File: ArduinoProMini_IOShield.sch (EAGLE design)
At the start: 29 parts, among them J0 POWER_JACKSLT, J1 Analog, J14 AVR_SPI_PROG_3X2PTH, J2 VCC-Analog, J3 GND-Analog, J4 Digital 0-7, J5 VCC_Digital, J6 GND-Digital, J7 Digital 8-13, J8 VCC-Digital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

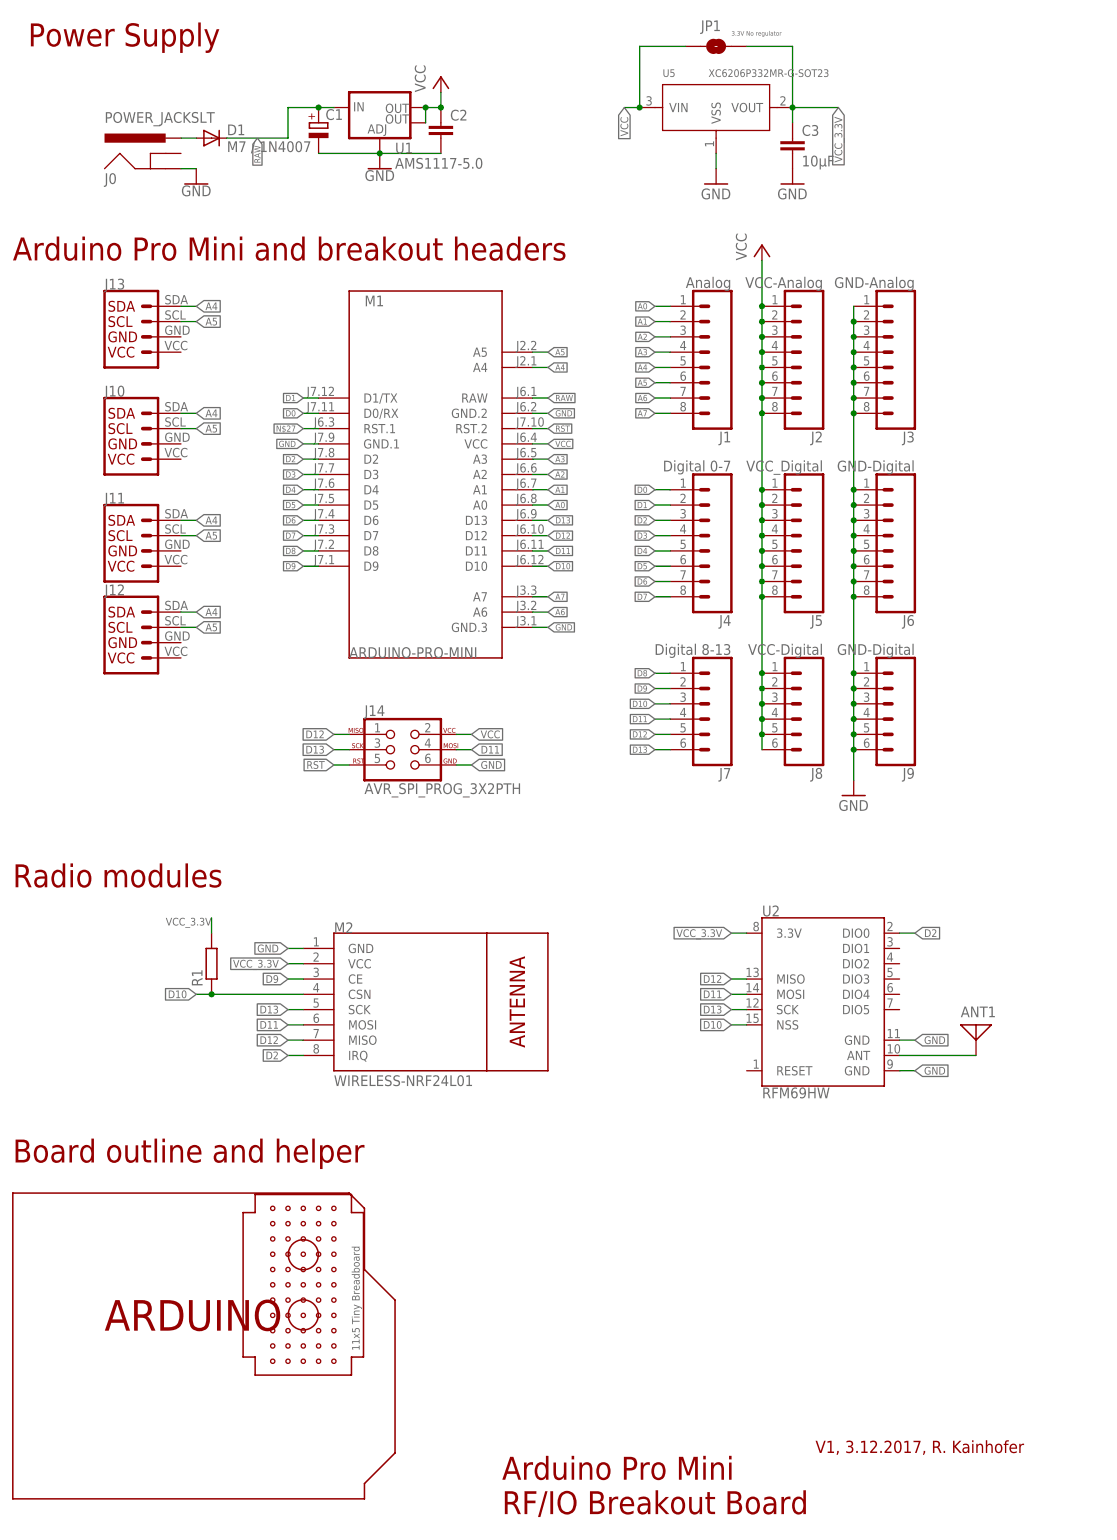
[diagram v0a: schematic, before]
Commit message: V0.2: Add power soldering connection, add altenative ProMini pinout, move ICSP header; Add pictures;
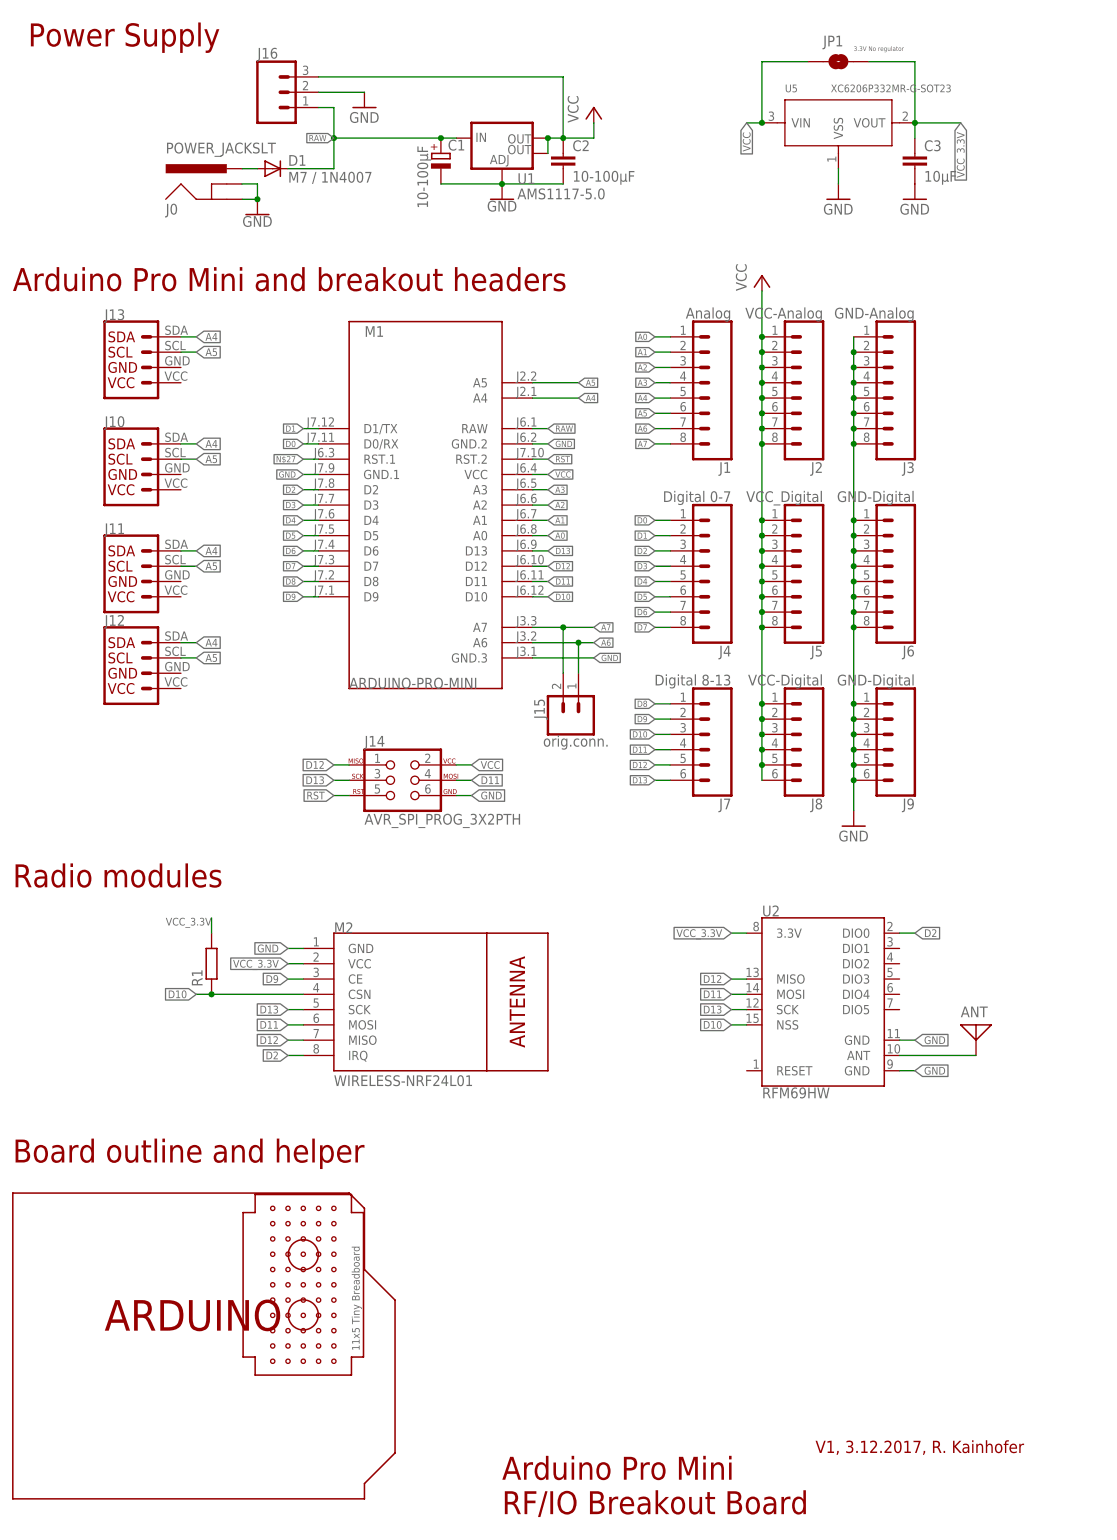
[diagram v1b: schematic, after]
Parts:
- added J15: orig.conn., SparkFun-Connectors:CONN_02
- added J16: (no value), SparkFun-Connectors:CONN_031X03_NO_SILK
- C1, C2: value (none) -> 10-100µF
- renumbered ANT1 to ANT
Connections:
- net A6: now also J15.1
- net A7: now also J15.2
- net GND: now also J0.GNDBREAK, J16.2
- net RAW: now also J16.1
- net VCC: now also J16.3
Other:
- moved on the sheet: C1, C2, C3, D1, J0, J1, J10, J11, J12, J13, J14, J2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
